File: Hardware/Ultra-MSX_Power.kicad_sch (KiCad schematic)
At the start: 70 parts, among them J10-0 ATX-24-LRJ, J10-1 Conn_KLDX-0202-A, U1 MPU_Z380, U10 SST39SF040, U14 SN74ABTH16244DL, U15 SN74ABT241APW, U2 AT40K10-2DQU, U4 YM2610, U5 BQ4802YPW, U6 74ABT245PW_118, U8 AS6C4008-55STIN, U9 DAC_YM3016

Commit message: Added cooler and CPU-mount footprints, as well as Indication LEDs.
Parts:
- removed L1, L2, L3, L4: L_Small, Ultra-MSX:Res_762, symbol Device:L_Small
- removed U8: AS6C4008-55STIN, Ultra-MSX:sTSOP-32_13.4x8mm_P0.5mm, symbol LRJ-parts:AS6C4008-55STIN
- added C14, C29: C_GRM32EC81C476KE15K, Capacitor_SMD:C_1210_3225Metric, symbol LRJ-parts:C_GRM32EC81C476KE15K
- added C67: C_CC0805JPX7R9BB104, Capacitor_SMD:C_0805_2012Metric, symbol LRJ-parts:C_CC0805JPX7R9BB104
- added C71: C_GRM21BR71A106KA73K, Capacitor_SMD:C_0805_2012Metric_Pad1.18x1.45mm_HandSolder, symbol LRJ-parts:C_GRM21BR71A106KA73K
- added D1, D2: LED_VLMW1300, LED_SMD:LED_0603_1608Metric, symbol LRJ-parts:LED_VLMW1300
- added D3, D4: LED_VLMB1310, LED_SMD:LED_0603_1608Metric, symbol LRJ-parts:LED_VLMB1310
- added L1, L2, L3, L4: DFE252012P-3R3M=P2, Inductor_SMD:L_1008_2520Metric, symbol LRJ-parts:DFE252012P-3R3M=P2
- added NT1, NT2: NetTie_2, NetTie:NetTie-2_SMD_Pad0.5mm, symbol Device:NetTie_2
- added R19: R_ERJ-3EKF1300V, Resistor_SMD:R_0603_1608Metric, symbol LRJ-parts:R_ERJ-3EKF1300V
- added R44: R_ERJ-3EKF10R0V, Resistor_SMD:R_0603_1608Metric, symbol LRJ-parts:R_ERJ-3EKF10R0V
- added R45, R46: R_ERJ-3GEYJ182V, Resistor_SMD:R_0603_1608Metric, symbol LRJ-parts:R_ERJ-3GEYJ182V
- added U16: AT40K10-2DQU, Package_QFP:PQFP-208_28x28mm_P0.5mm, symbol LRJ-parts:AT40K10-2DQU
- added U8: AS6C8008-55ZIN, Package_SO:TSOP-II-44_10.16x18.41mm_P0.8mm, symbol LRJ-parts:AS6C8008-55ZIN
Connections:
- net +12V: now also L1.1, R45.1
- net +12VA: now also L1.2
- net +3.3V: now also C14.1, C29.1, R44.2
- net +5V: now also C67.1, C71.1, L3.1, NT1.1, R19.1, U16.106 (VCC), U16.130 (VCC), U16.154 (VCC), U16.183 (VCC), U16.205 (VCC), U16.26 (VCC), U16.55 (VCC), U16.78 (VCC), U8.33 (VCC)
- net -12V: now also L2.1, R46.1
- net -12VA: now also L2.2
- net GND: now also C67.2, C71.2, NT2.1, U16.101 (GND), U16.119 (GND), U16.131 (GND), U16.14 (GND), U16.142 (GND), U16.160 (GND), U16.171 (GND), U16.182 (GND), U16.194 (GND), U16.2 (GND), U16.25 (GND), U16.37 (GND), U16.49 (GND), U16.67 (GND), U16.79 (GND), U16.90 (GND), U8.34 (VSS)
- net GNDPWR1: now also C14.2, C29.2, D1.1 (K), D2.1 (K), D3.1 (K), D4.1 (K)
- net VCC_DAC: now also L4.2
- net VCC_PSG: now also L3.2, L4.1
- new net +12D4: D1.2 (A), R45.2
- new net +3.3D3: D4.2 (A), R44.1
- new net +5D2: D3.2 (A), R19.2
- new net -12D1: D2.2 (A), R46.2
- new net GND/SBU2: NT2.2
- new net VCT/SBU1: NT1.2
- now unconnected: U2.1 (N/C), U2.102 (N/C), U2.104 (N/C), U2.105 (N/C), U2.107 (N/C), U2.155 (N/C), U2.156 (N/C), U2.157 (N/C), U2.158 (N/C), U2.206 (N/C), U2.207 (N/C), U2.208 (N/C), U2.3 (N/C), U2.51 (N/C), U2.52 (N/C), U2.53 (N/C), U2.54 (N/C)
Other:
- note added: "IO-extender Power"
- note added: "LED power-indication"
- note added: "Power-use Calculation: ---------------------- 12V: ------ Wave: MIDI: A_AMP(x7): ------ 5V: ------ CPU: 20 mA MSXE: 40 mA IOE: RAM: BUF(x3): WD: ROM: CAS_AMP: CAS_RY: AUD: ---- 2610: VT(x4): Sample: RV(x4): A_DAC: ---- ------"
- moved on the sheet: C1, C101, C102, C103, C104, C105, C106, C107, C108, C11, C13, C15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

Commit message: Started fixing many small issues.
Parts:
- removed C20, C62: C, Capacitor_SMD:C_0603_1608Metric, symbol Device:C
- removed NT1, NT2: NetTie_2, NetTie:NetTie-2_SMD_Pad0.5mm, symbol Device:NetTie_2
- removed U16: AT40K10-2DQU, Package_QFP:PQFP-208_28x28mm_P0.5mm, symbol LRJ-parts:AT40K10-2DQU
- added C100, C117, C121, C122, C41, C84: C_GRM21BR71A106KA73K, Capacitor_SMD:C_0805_2012Metric_Pad1.18x1.45mm_HandSolder, symbol LRJ-parts:C_GRM21BR71A106KA73K
- added C118, C119, C120, C20, C31, C40, C42, C62, C96: C_CC0805JPX7R9BB104, Capacitor_SMD:C_0805_2012Metric, symbol LRJ-parts:C_CC0805JPX7R9BB104
- added RV5: AD5144ABRUZ100, Package_SO:TSSOP-20_4.4x6.5mm_P0.65mm, symbol LRJ-parts:AD5144ABRUZ100
- added U23: S29GL128S90TFI010, Package_SO:TSOP-I-56_18.4x14mm_P0.5mm, symbol LRJ-parts:S29GL128S90TFI010
- added U3: AT40K10-2DQU, Package_QFP:PQFP-208_28x28mm_P0.5mm, symbol LRJ-parts:AT40K10-2DQU
- added trace1: pcb-trace, LRJ:NetTie-2_SMD_Pad0.2mm, symbol LRJ-parts:Trace
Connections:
- net GNDA is gone; now on net GND: C101.2, C102.1, C102.2, C103.2, C104.1, C104.2, C105.2, C106.1, C106.2, C107.2, C108.1, C108.2, C13.2, C36.2, C37.1, C37.2, C63.2, C66.2, C95.1, C95.2, C97.2, C98.1, C98.2, C99.1, C99.2, RV1.9 (V_{SS}), RV2.9 (V_{SS}), RV3.9 (V_{SS}), RV4.9 (V_{SS}), U4.26 (GNDA)
- net GNDPWR1 is gone; now on net GND: C14.2, C28.2, C29.2, C30.2, C32.1, C33.1, C34.1, C39.1, D1.1 (K), D2.1 (K), D3.1 (K), D4.1 (K), J10-0.15 (GND), J10-0.17 (GND), J10-0.18 (GND), J10-0.19 (GND), J10-0.24 (GND), J10-0.3 (GND), J10-0.5 (GND), J10-0.7 (GND)
- net GNDPWR2 is gone; now on net GND: C68.1, C69.1, J10-1.2, J10-1.3
- net +12V: now also C31.1
- net +3.3V: now also C100.1, C96.1
- net +5D2: now also trace1.2
- net +5V: now also C117.1, C118.1, C20.1, C41.1, C42.1, RV5.17 (V_{LOGIC}), U3.106 (VCC), U3.130 (VCC), U3.154 (VCC), U3.183 (VCC), U3.205 (VCC), U3.26 (VCC), U3.55 (VCC), U3.78 (VCC)
- net +5VSB: now also C62.1, C84.1
- net -12V: now also C40.2
- net GND: now also C100.2, C117.2, C118.2, C119.2, C120.1, C120.2, C121.2, C122.1, C122.2, C20.2, C31.2, C40.1, C41.2, C42.2, C62.2, C84.2, C96.2, RV5.2 (GND), RV5.9 (V_{SS}), U3.101 (GND), U3.119 (GND), U3.131 (GND), U3.14 (GND), U3.142 (GND), U3.160 (GND), U3.171 (GND), U3.182 (GND), U3.194 (GND), U3.2 (GND), U3.25 (GND), U3.37 (GND), U3.49 (GND), U3.67 (GND), U3.79 (GND), U3.90 (GND)
- net VCC_DAC: now also C119.1, C121.1, RV5.16 (V_{DD})
- new net PLED+: trace1.1
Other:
- note added: "+5VP"
- note added: "+5VSB"
- note added: "/PS_ON"
- note added: "= Analog ground."
- note added: "= External five volts from the FPGA-programmer."
- note added: "= Standby-signal - supplies power when other lines are off. can be used to power the device sending PS_ON."
- note added: "= from Motherboard - when PSU is on, this line will be grounded by a device on the Motheboard."
- note added: "= output from PSU, indicating that power-out has stabilized."
- note added: "= the incoming Ground from the PSU(s) connected to the board."
- note added: "ATX Decoupling"
- note added: "Audio ROM Power"
- note added: "GNDA"
- note added: "GNDPWR1,2"
- note added: "LEGEND: -------"
- note added: "PWR_OK"
- note added: "VCT = VCC Target (device to be programmed by JTAG)"
- note removed: "LEGEND: ------- /PS_ON = from MB - when PSU is on, this line will be grounded by a device on the MB. PWR_OK = output from PSU, indicating that power-out has stabilized +5 VSB = Standby - supplies power when other lines are off. can be used to power the device sending PS_ON. GNDA = Analog ground. GNDPWR1,2 = the incoming Ground from the PSU(s) connected to the board. +5VP = External five volts fro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"
- note removed: "Main Decoupling"
- note removed: "VCC_ROM"
- moved on the sheet: C1, C101, C102, C103, C104, C105, C106, C107, C108, C11, C13, C14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

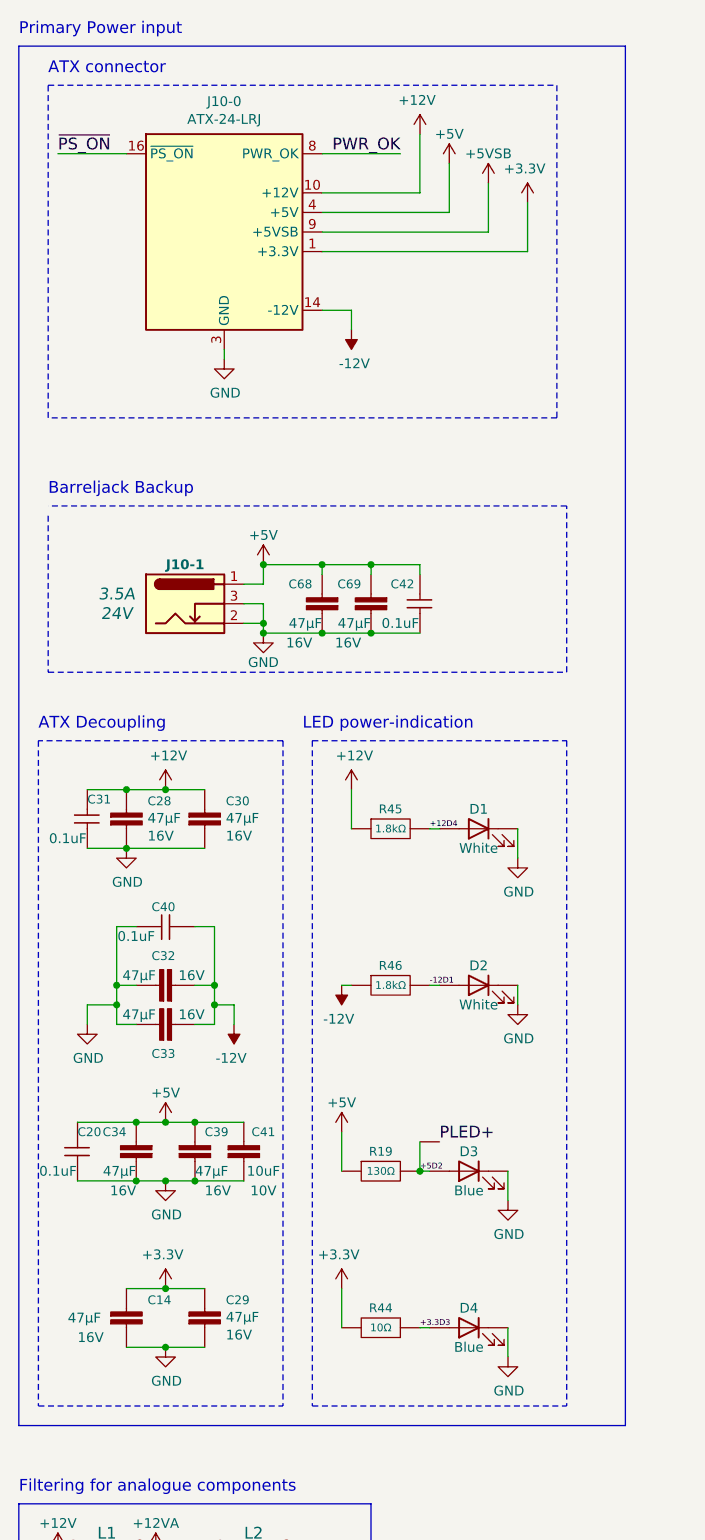
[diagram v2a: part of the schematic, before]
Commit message: Updated the readme, silenced multiple errors in Kicad regarding simulation-files.
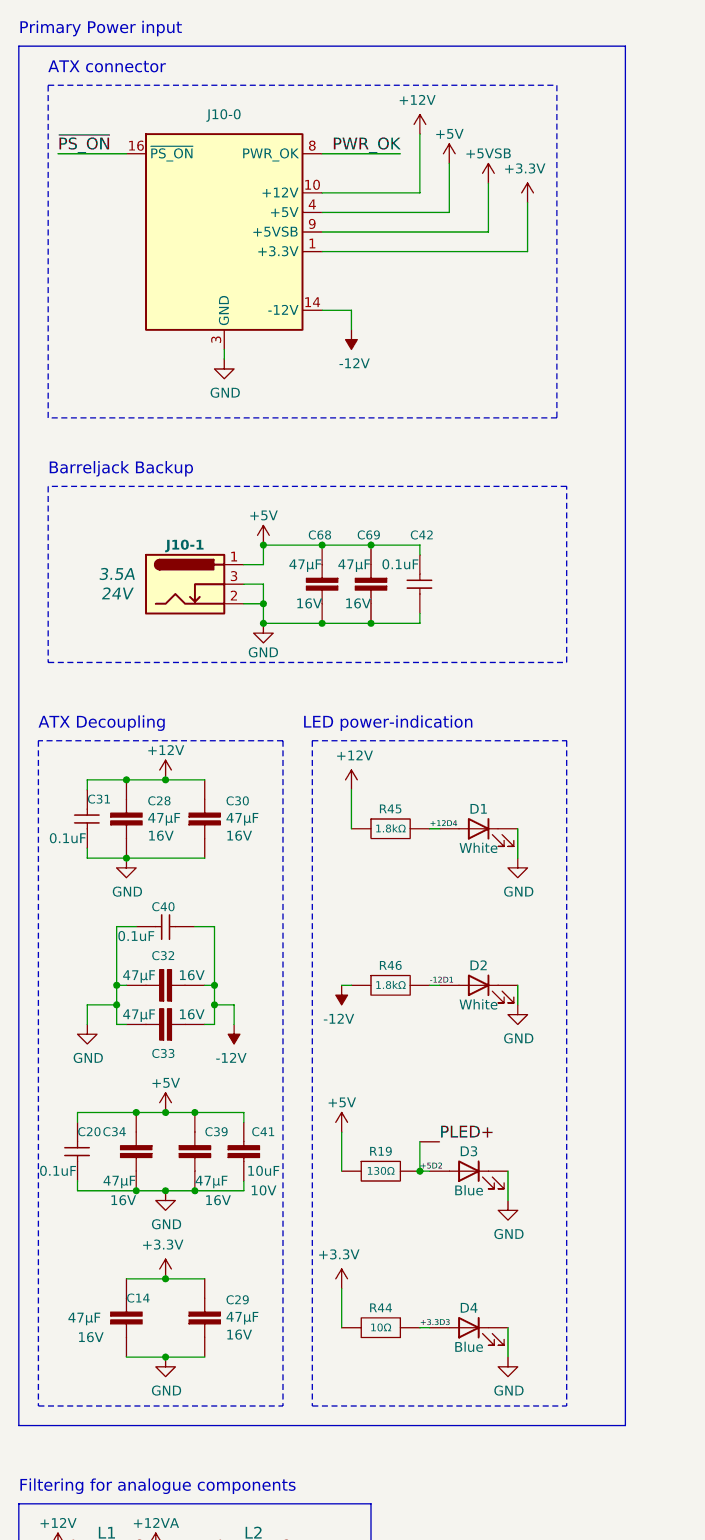
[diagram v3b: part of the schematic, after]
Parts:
- removed J10-0: ATX-24-LRJ, LRJ:Molex_Mini-Fit_Jr_5566-24A2_2x12_P4.20mm_Vertical, symbol Ultra-MSX:ATX-24-LRJ
- removed trace1: pcb-trace, LRJ:NetTie-2_SMD_Pad0.2mm, symbol LRJ-parts:Trace
- added J10-0: Molex_0469990346, LRJ:Molex_Mini-Fit_Jr_5566-24A2_2x12_P4.20mm_Vertical, symbol Ultra-MSX:Molex_0469990346
- added trace1: pcb-trace, LRJ:NetTie-2_SMD_Pad0.2mm, symbol LRJ-parts:Trace_0.2mm
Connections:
- net +12V: now also J10-0.10 (+12V), J10-0.11 (+12V)
- net +3.3V: now also J10-0.1 (+3.3V), J10-0.12 (+3.3V), J10-0.13 (+3.3V), J10-0.2 (+3.3V)
- net +5D2: now also trace1.2
- net +5V: now also J10-0.21 (+5V), J10-0.22 (+5V), J10-0.23 (+5V), J10-0.4 (+5V), J10-0.6 (+5V)
- net +5VSB: now also J10-0.9 (+5VSB)
- net -12V: now also J10-0.14 (-12V)
- net GND: now also J10-0.15 (GND), J10-0.17 (GND), J10-0.18 (GND), J10-0.19 (GND), J10-0.24 (GND), J10-0.3 (GND), J10-0.5 (GND), J10-0.7 (GND)
- net PLED+: now also trace1.1
- net PWR_OK: now also J10-0.8 (PWR_OK)
- net ~{PS_ON}: now also J10-0.16 (~{PS_ON})
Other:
- moved on the sheet: C42, C68, C69, J10-1

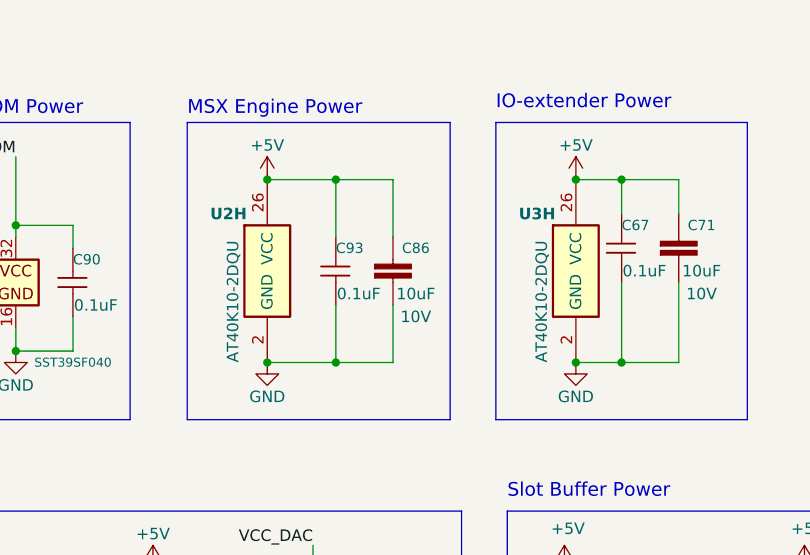
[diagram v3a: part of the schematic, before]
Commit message: Many tweaks and changes, such as a slight redesign of the VDP-baord.
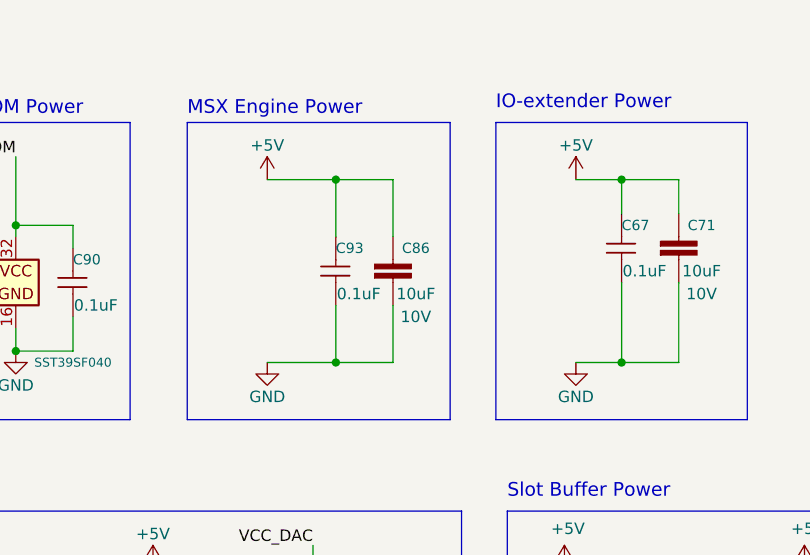
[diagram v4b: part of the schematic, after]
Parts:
- removed U2, U3: AT40K10-2DQU, Package_QFP:PQFP-208_28x28mm_P0.5mm, symbol LRJ-parts:AT40K10-2DQU

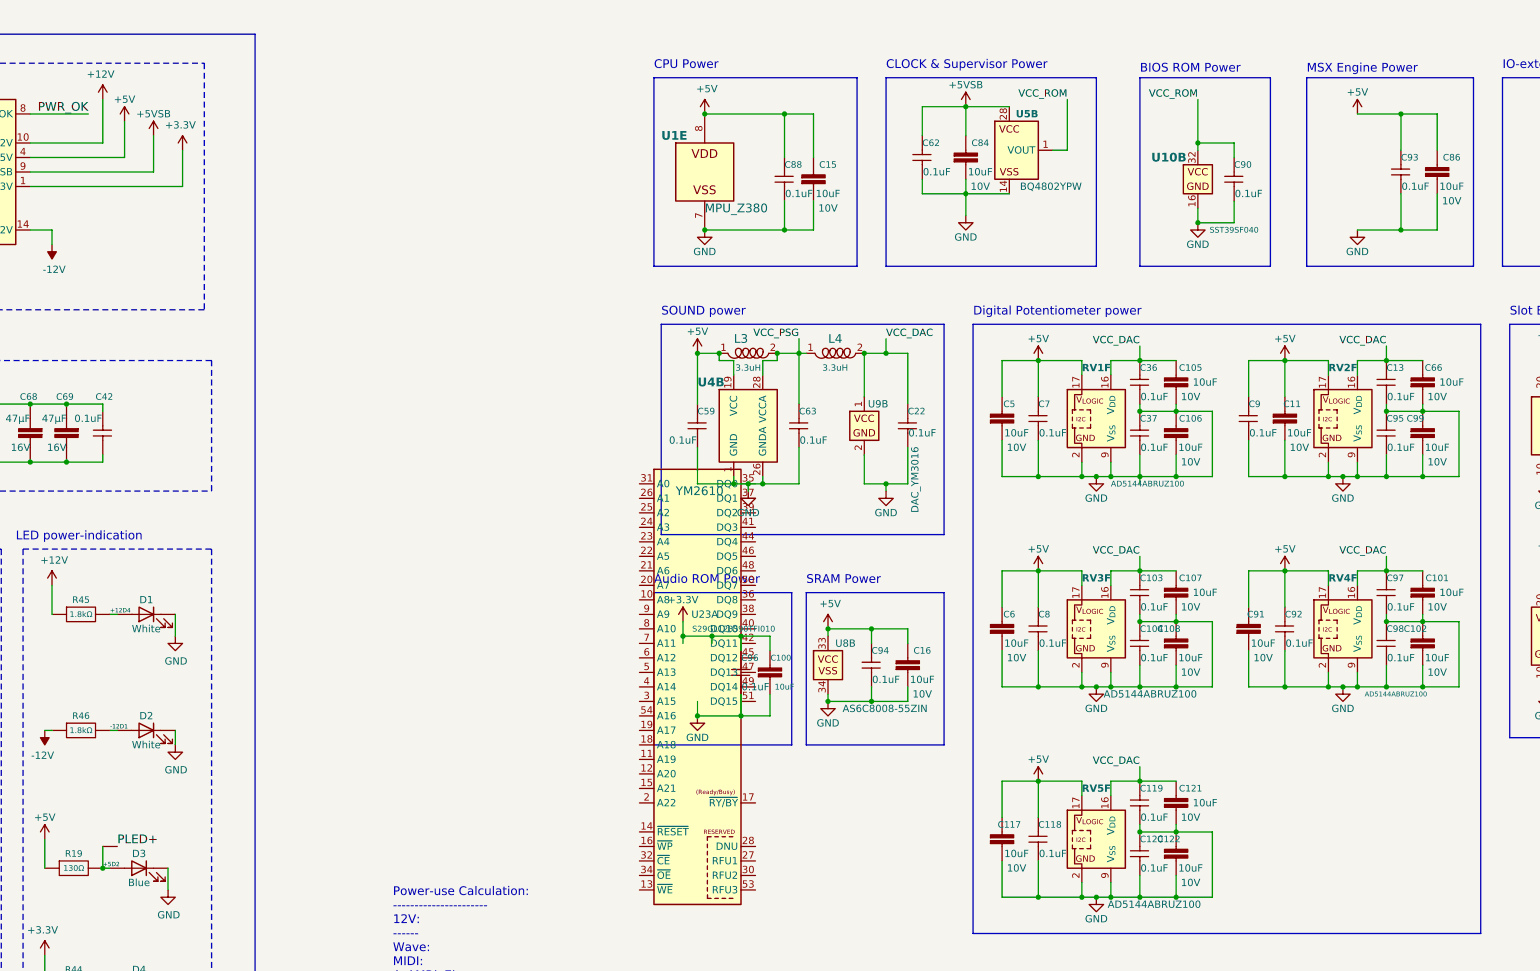
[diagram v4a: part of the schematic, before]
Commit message: Returned to Simm-72 memory module to simplify design, returned to AT40K40 with 254 io, FPGA.
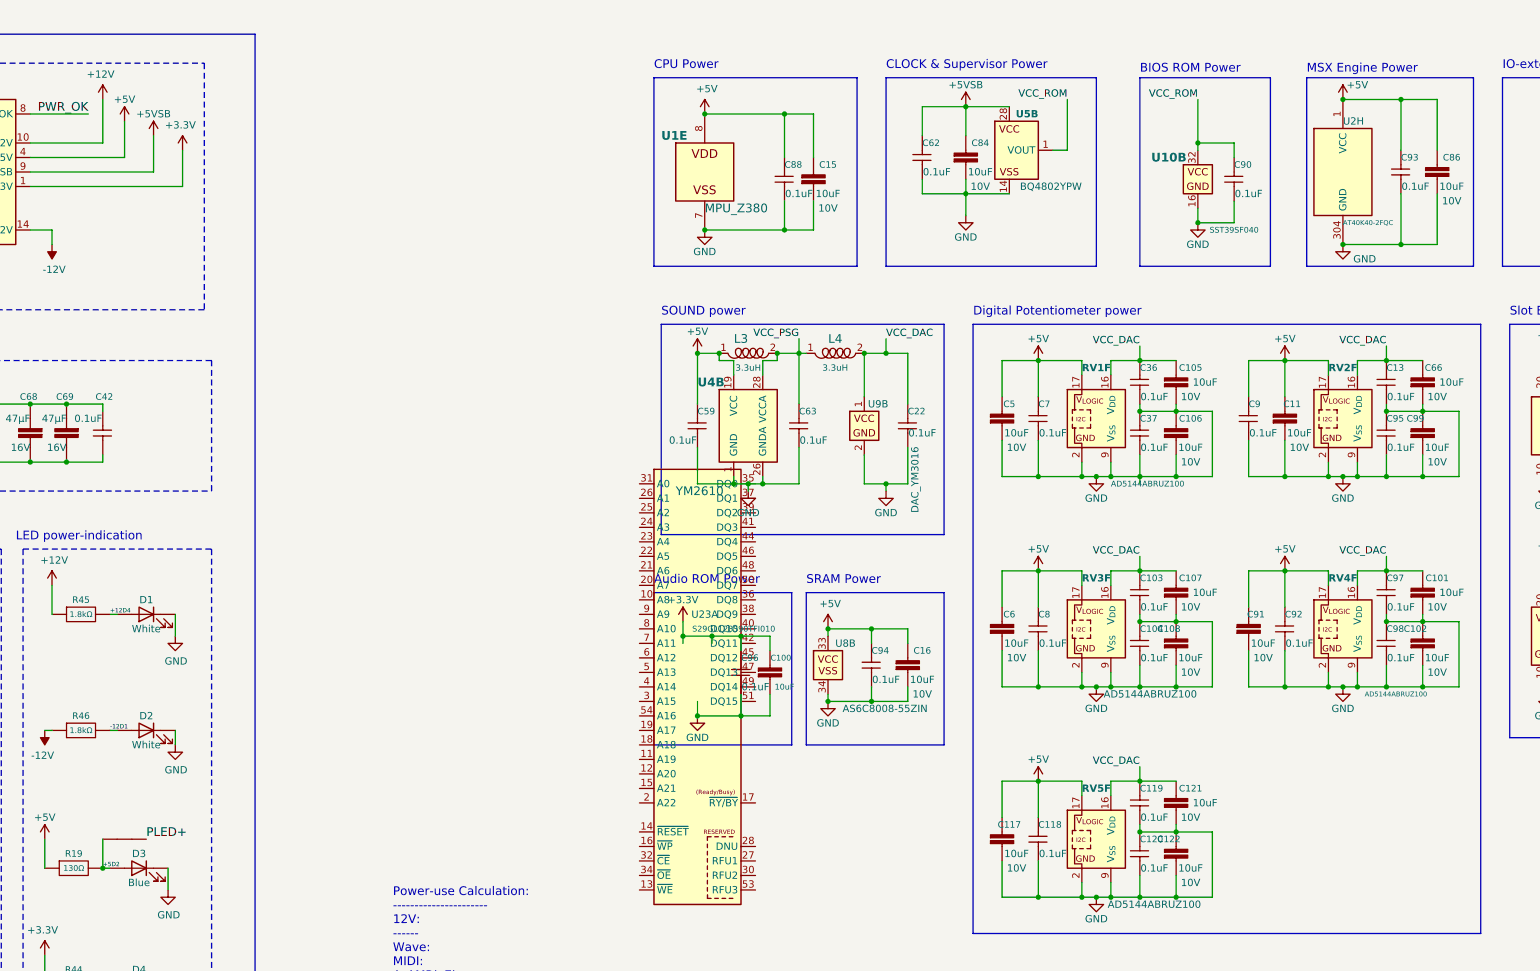
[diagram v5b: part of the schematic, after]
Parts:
- added U2: AT40K40-2FQC, LRJ:PQFP-304_40x40mm_P0.5mm, symbol LRJ-parts:AT40K40-2FQC
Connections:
- net +5V: now also U2.1 (VCC), U2.101 (VCC), U2.115 (VCC), U2.129 (VCC), U2.152 (VCC), U2.177 (VCC), U2.191 (VCC), U2.204 (VCC), U2.228 (VCC), U2.25 (VCC), U2.253 (VCC), U2.267 (VCC), U2.282 (VCC), U2.38 (VCC), U2.52 (VCC), U2.77 (VCC)
- net GND: now also U2.114 (GND), U2.134 (GND), U2.154 (GND), U2.171 (GND), U2.19 (GND), U2.190 (GND), U2.210 (GND), U2.230 (GND), U2.248 (GND), U2.268 (GND), U2.287 (GND), U2.304 (GND), U2.39 (GND), U2.58 (GND), U2.75 (GND), U2.95 (GND)
